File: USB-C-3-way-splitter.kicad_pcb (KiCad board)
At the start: 2 copper layers, 33 x 33 mm, 25 parts, among them J1 USB_C_Receptacle_USB2.0, J2 Conn_01x05_Socket, J3 Conn_01x05_Socket, J4 Conn_01x05_Socket, U1 LM393

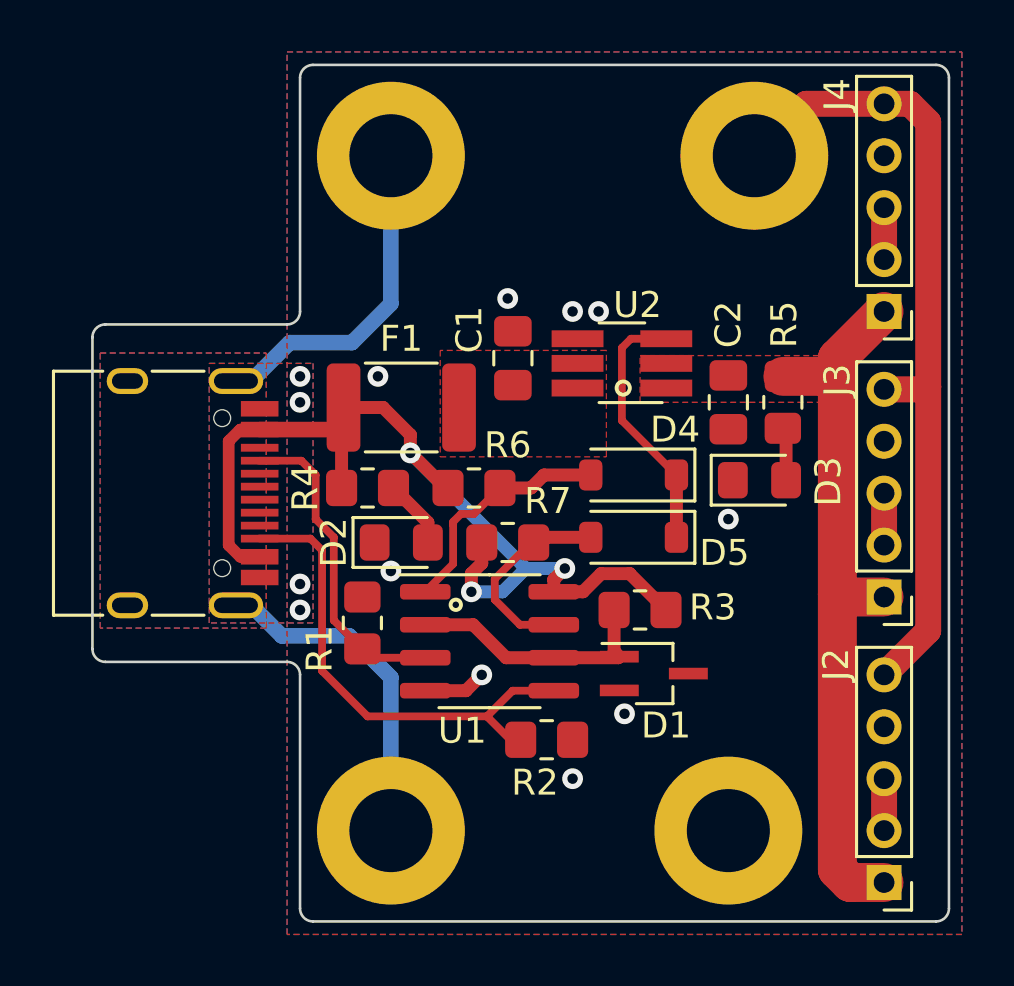
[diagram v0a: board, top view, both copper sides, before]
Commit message: Moved everything on the 5v rail to after the fuse
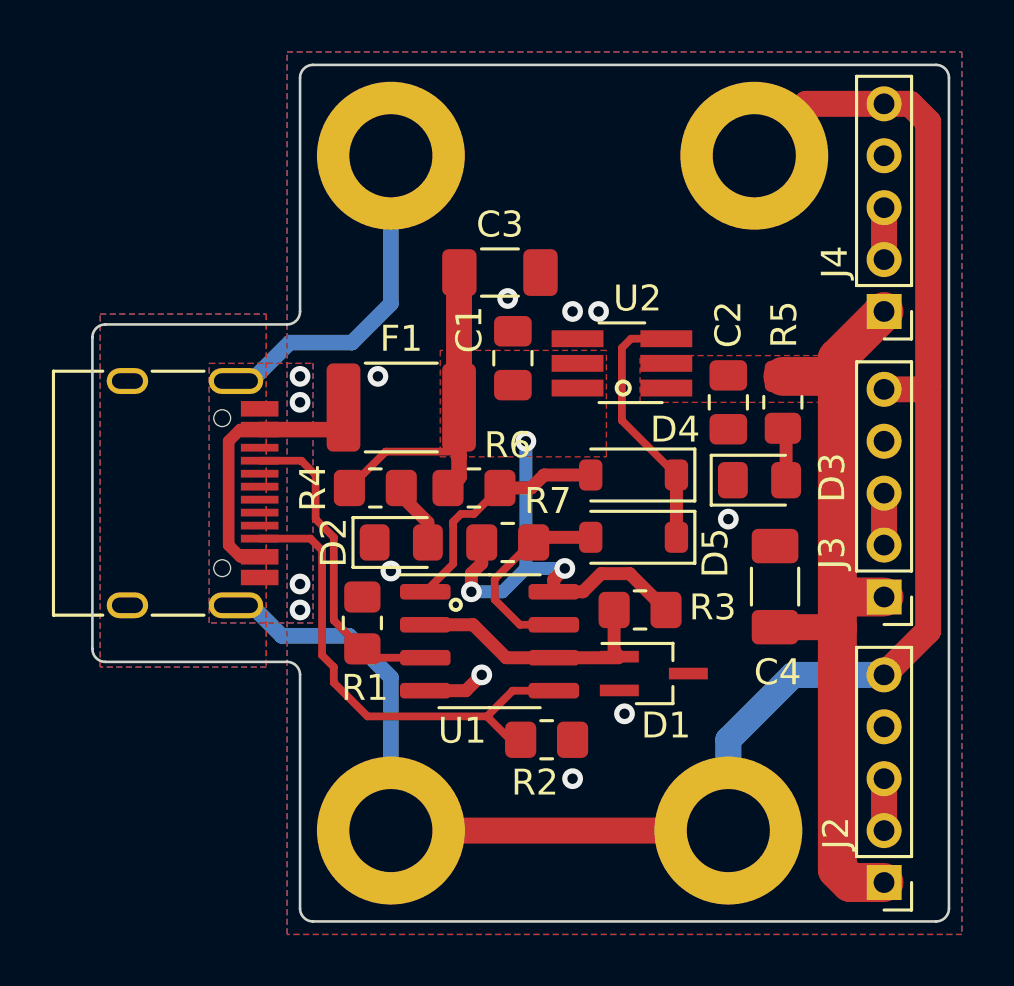
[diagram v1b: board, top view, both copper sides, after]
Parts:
- added C3: 22uF, Capacitor_SMD:C_1206_3216Metric_Pad1.33x1.80mm_HandSolder, F.Cu at (14.2, -8.50)
- added C4: 22uF, Capacitor_SMD:C_1206_3216Metric_Pad1.33x1.80mm_HandSolder, F.Cu at (24.8, 3.60)
- moved R4 0.30 mm to (9.40, -0.20)
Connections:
- C1 pad 1: Net-(C1-Pad1) -> VBUS
- F1 pad 1: VBUS -> Net-(F1-Pad1)
- F1 pad 2: Net-(C1-Pad1) -> VBUS
- J1 pad A4: VBUS -> Net-(F1-Pad1)
- J1 pad A6: D+ -> unconnected-(J1-D+-PadA6)
- J1 pad A7: D- -> unconnected-(J1-D--PadA7)
- J1 pad A9: VBUS -> Net-(F1-Pad1)
- J1 pad B4: VBUS -> Net-(F1-Pad1)
- J1 pad B6: D+ -> unconnected-(J1-D+-PadB6)
- J1 pad B7: D- -> unconnected-(J1-D--PadB7)
- J1 pad B9: VBUS -> Net-(F1-Pad1)
- U2 pad 5: Net-(C1-Pad1) -> VBUS
- U2 pad 6: Net-(C1-Pad1) -> VBUS
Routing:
- net GNDPWR: track 57.5 -> 81.0 mm
- net Net-(F1-Pad1): track 0.00 -> 11.0 mm
- net VBUS: track 38.3 -> 30.6 mm
- net +5V: track 28.3 -> 30.7 mm
- added copper zone on F.Cu, net VBUS
- removed copper zone on F.Cu, net Net-(C1-Pad1)
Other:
- board text added: "+5V"
- board text added: "D+"
- board text added: "D-"
- board text added: "GND"
- board text added: "SHIELD"

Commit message: Never mind misunderstood the LM393M's behavior
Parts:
- R6, R7: value R -> 1k
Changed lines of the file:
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@@
         (effects (font (size 1 1) (thickness 0.15)))
     )
-    (fp_text value "R" (at 0 1.65) (layer "F.Fab")
+    (fp_text value "1k" (at 0 1.65) (layer "F.Fab")
         (effects (font (size 1 1) (thickness 0.15)))
     )
@@
         (effects (font (size 1 1) (thickness 0.15)))
     )
-    (fp_text value "R" (at 0 1.65) (layer "F.Fab")
-        (effects (font (size 1 1) (thickness 0.15)))
-    )
+    (fp_text value "1k" (at 0 1.65) (layer "F.Fab")
+        (effects (font (size 1 1) (thickness 0.15)))
+    )

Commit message: Design is done maybe?
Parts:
- added C5: 100nF, Capacitor_SMD:C_0805_2012Metric_Pad1.18x1.45mm_HandSolder, F.Cu at (24.6, 7.30)
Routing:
- net +1V2: track 9.90 -> 15.3 mm
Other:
- board text added: "JLCJLCJLCJLC"
- board text added: "USB-C Splitter V1 Pylon Feb 14 24"
- board text removed: "USB-C Splitter V1 Pylon Feb 13 24"
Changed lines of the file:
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@@
     (property "ki_keywords" "cap capacitor")
     (attr smd)
-    (fp_text reference "C4" (at -3.3 0.1 180) (layer "F.SilkS")
+    (fp_text reference "C4" (at -0.7 2 270) (layer "F.SilkS")
         (effects (font (size 1 1) (thickness 0.15)))
     )
@@
       (net 1 "GND") (pintype "passive"))
     (model "${KICAD6_3DMODEL_DIR}/Resistor_SMD.3dshapes/R_0805_2012Metric.wrl"
+      (offset (xyz 0 0 0))
+      (scale (xyz 1 1 1))
+      (rotate (xyz 0 0 0))
+    )
+  )
+  (footprint "Capacitor_SMD:C_0805_2012Metric_Pad1.18x1.45mm_HandSolder" (layer "F.Cu")
+    (at 24.6 7.3)
+    (descr "Capacitor SMD 0805 (2012 Metric), square (rectangular) end terminal, IPC_7351 nominal with elongated pad for handsoldering. (Body size source: IPC-SM-782 page 76, https://www.pcb-3d.com/wordpress/wp-content/uploads/ipc-sm-782a_amendment_1_and_2.pdf, https://docs.google.com/spreadsheets/d/1BsfQQcO9C6DZCsRaXUlFlo91Tg2WpOkGARC1WS5S8t0/edit?usp=sharing), generated with kicad-footprint-generator")
+    (tags "capacitor handsolder")
+    (property "Sheetfile" "USB-C-3-way-splitter.kicad_sch")
+    (property "Sheetname" "")
+    (property "ki_description" "Unpolarized capacitor")
+    (property "ki_keywords" "cap capacitor")
+    (attr smd)
+    (fp_text reference "C5" (at 0.595 1.695) (layer "F.SilkS")
+        (effects (font (size 1 1) (thickness 0.15)))
+    )
+    (fp_text value "100nF" (at 0 1.68) (layer "F.Fab")
+        (effects (font (size 1 1) (thickness 0.15)))
+    )
+    (fp_text user "${REFERENCE}" (at 0 0) (layer "F.Fab")
+        (effects (font (size 0.5 0.5) (thickness 0.08)))
+    )
+    (fp_line (start -0.261252 -0.735) (end 0.261252 -0.735)
+      (stroke (width 0.12) (type solid)) (layer "F.SilkS"))
+    (fp_line (start -0.261252 0.735) (end 0.261252 0.735)
+      (stroke (width 0.12) (type solid)) (layer "F.SilkS"))
+    (fp_line (start -1.88 -0.98) (end 1.88 -0.98)
+      (stroke (width 0.05) (type solid)) (layer "F.CrtYd"))
+    (fp_line (start -1.88 0.98) (end -1.88 -0.98)
+      (stroke (width 0.05) (type solid)) (layer "F.CrtYd"))
+    (fp_line (start 1.88 -0.98) (end 1.88 0.98)
+      (stroke (width 0.05) (type solid)) (layer "F.CrtYd"))
+    (fp_line (start 1.88 0.98) (end -1.88 0.98)
+      (stroke (width 0.05) (type solid)) (layer "F.CrtYd"))
+    (fp_line (start -1 -0.625) (end 1 -0.625)
+      (stroke (width 0.1) (type solid)) (layer "F.Fab"))
+    (fp_line (start -1 0.625) (end -1 -0.625)
+      (stroke (width 0.1) (type solid)) (layer "F.Fab"))
+    (fp_line (start 1 -0.625) (end 1 0.625)
+      (stroke (width 0.1) (type solid)) (layer "F.Fab"))
+    (fp_line (start 1 0.625) (end -1 0.625)
+      (stroke (width 0.1) (type solid)) (layer "F.Fab"))
+    (pad "1" smd roundrect (at -1.0375 0) (size 1.175 1.45) (layers "F.Cu" "F.Paste" "F.Mask") (roundrect_rratio 0.212766)
+      (net 8 "+1V2") (pintype "passive"))
+    (pad "2" smd roundrect (at 1.0375 0) (size 1.175 1.45) (layers "F.Cu" "F.Paste" "F.Mask") (roundrect_rratio 0.212766)
+      (net 1 "GND") (pintype "passive"))
+    (model "${KICAD6_3DMODEL_DIR}/Capacitor_SMD.3dshapes/C_0805_2012Metric.wrl"
       (offset (xyz 0 0 0))
       (scale (xyz 1 1 1))
@@
   (gr_arc (start -1 6.5) (mid -1.353553 6.353553) (end -1.5 6)
     (stroke (width 0.1) (type default)) (layer "Edge.Cuts"))
+  (gr_text "JLCJLCJLCJLC" (at 21.5 -6.3 90) (layer "B.SilkS")
+    (effects (font (size 1 1) (thickness 0.2) bold) (justify left bottom mirror))
+  )
   (gr_text "+5V" (at 27.9 4.5) (layer "B.SilkS")
     (effects (font (size 1 1) (thickness 0.2) bold) (justify left bottom mirror))
@@
     (effects (font (size 1 1) (thickness 0.2) bold) (justify left bottom mirror))
   )
-  (gr_text "USB-C Splitter V1\nPylon Feb 13 24" (at 16.6 -10.5 90) (layer "B.SilkS")
+  (gr_text "USB-C Splitter V1\nPylon Feb 14 24" (at 16.6 -10.5 90) (layer "B.SilkS")
     (effects (font (size 1.5 1.5) (thickness 0.3) bold) (justify left bottom mirror))
   )
@@
   (segment (start 18.76 6.34) (end 18.8 6.3) (width 0.5) (layer "F.Cu") (net 8))
   (segment (start 16.275 6.34) (end 18.76 6.34) (width 0.5) (layer "F.Cu") (net 8))
+  (segment (start 22.2625 6) (end 23.5625 7.3) (width 0.5) (layer "F.Cu") (net 8))
+  (segment (start 18.8 6.3) (end 20 6.3) (width 0.5) (layer "F.Cu") (net 8))
   (segment (start 18.6 6.1) (end 18.8 6.3) (width 0.5) (layer "F.Cu") (net 8))
+  (segment (start 20 6.3) (end 20.3 6) (width 0.5) (layer "F.Cu") (net 8))
   (segment (start 11.325 5.07) (end 13.17 5.07) (width 0.5) (layer "F.Cu") (net 8))
   (segment (start 14.44 6.34) (end 16.275 6.34) (width 0.5) (layer "F.Cu") (net 8))
+  (segment (start 20.3 6) (end 22.2625 6) (width 0.5) (layer "F.Cu") (net 8))
   (segment (start 13.17 5.07) (end 14.44 6.34) (width 0.5) (layer "F.Cu") (net 8))
   (segment (start 11.425 1.125) (end 11.425 1.9) (width 0.5) (layer "F.Cu") (net 9))

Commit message: Added JLCPCB tooling holes
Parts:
- added H5: MountingHole, USB-C-3-way-splitter-footprints:JLCPCB-tooling-hole, F.Cu at (14.5, -15.0)
- added H6: MountingHole, USB-C-3-way-splitter-footprints:JLCPCB-tooling-hole, F.Cu at (14.0, 15.0)
- added H7: MountingHole, USB-C-3-way-splitter-footprints:JLCPCB-tooling-hole, F.Cu at (26.0, -8.00)
- U2: value ~ -> SiP32509
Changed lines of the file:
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@@
     )
+  )
+  (footprint "USB-C-3-way-splitter-footprints:JLCPCB-tooling-hole" (layer "F.Cu")
+    (at 26 -8)
+    (property "Sheetfile" "USB-C-3-way-splitter.kicad_sch")
+    (property "Sheetname" "")
+    (property "ki_description" "Mounting Hole without connection")
+    (property "ki_keywords" "mounting hole")
+    (attr smd)
+    (fp_text reference "H7" (at 0 -2 unlocked) (layer "User.1")
+        (effects (font (size 1 1) (thickness 0.1)))
+    )
+    (fp_text value "MountingHole" (at 0 1 unlocked) (layer "F.Fab")
+        (effects (font (size 1 1) (thickness 0.15)))
+    )
+    (fp_text user "${REFERENCE}" (at 0 2.5 unlocked) (layer "F.Fab")
+        (effects (font (size 1 1) (thickness 0.15)))
+    )
+    (pad "" np_thru_hole circle (at 0 0) (size 2.286 2.286) (drill 1.152) (layers "F&B.Cu" "*.Mask")
+      (solder_mask_margin 0.148) (clearance 0.148))
   )
   (footprint "Diode_SMD:D_SOD-123" (layer "F.Cu")
@@
     (pad "1" thru_hole circle (at 0 0) (size 5.7 5.7) (drill 3.2) (layers "*.Cu" "*.Mask")
       (net 16 "GNDPWR") (pinfunction "1") (pintype "input"))
+  )
+  (footprint "USB-C-3-way-splitter-footprints:JLCPCB-tooling-hole" (layer "F.Cu")
+    (at 14 15)
+    (property "Sheetfile" "USB-C-3-way-splitter.kicad_sch")
+    (property "Sheetname" "")
+    (property "ki_description" "Mounting Hole without connection")
+    (property "ki_keywords" "mounting hole")
+    (attr smd)
+    (fp_text reference "H6" (at 0 -2 unlocked) (layer "User.1")
+        (effects (font (size 1 1) (thickness 0.1)))
+    )
+    (fp_text value "MountingHole" (at 0 1 unlocked) (layer "F.Fab")
+        (effects (font (size 1 1) (thickness 0.15)))
+    )
+    (fp_text user "${REFERENCE}" (at 0 2.5 unlocked) (layer "F.Fab")
+        (effects (font (size 1 1) (thickness 0.15)))
+    )
+    (pad "" np_thru_hole circle (at 0 0) (size 2.286 2.286) (drill 1.152) (layers "F&B.Cu" "*.Mask")
+      (solder_mask_margin 0.148) (clearance 0.148))
   )
   (footprint "Package_SO:SOIC-8_3.9x4.9mm_P1.27mm" (layer "F.Cu")
@@
         (effects (font (size 1 1) (thickness 0.15)))
     )
-    (fp_text value "~" (at 0 2.5) (layer "F.Fab")
+    (fp_text value "SiP32509" (at 0 2.5) (layer "F.Fab")
         (effects (font (size 1 1) (thickness 0.15)))
     )
@@
     (fp_line (start 1 0.625) (end -1 0.625)
       (stroke (width 0.1) (type solid)) (layer "F.Fab"))
-    (pad "1" smd roundrect (at -1.0375 0) (size 1.175 1.45) (layers "F.Cu" "F.Paste" "F.Mask") (roundrect_rratio 0.212766)
+    (pad "1" smd roundrect (at -1.0375 0) (size 1.175 1.45) (layers "F.Cu" "F.Paste" "F.Mask") (roundrect_rratio 0.2127659574)
       (net 8 "+1V2") (pintype "passive"))
-    (pad "2" smd roundrect (at 1.0375 0) (size 1.175 1.45) (layers "F.Cu" "F.Paste" "F.Mask") (roundrect_rratio 0.212766)
+    (pad "2" smd roundrect (at 1.0375 0) (size 1.175 1.45) (layers "F.Cu" "F.Paste" "F.Mask") (roundrect_rratio 0.2127659574)
       (net 1 "GND") (pintype "passive"))
     (model "${KICAD6_3DMODEL_DIR}/Capacitor_SMD.3dshapes/C_0805_2012Metric.wrl"
@@
     )
   )
+  (footprint "USB-C-3-way-splitter-footprints:JLCPCB-tooling-hole" (layer "F.Cu")
+    (at 14.5 -15)
+    (property "Sheetfile" "USB-C-3-way-splitter.kicad_sch")
+    (property "Sheetname" "")
+    (property "ki_description" "Mounting Hole without connection")
+    (property "ki_keywords" "mounting hole")
+    (attr smd)
+    (fp_text reference "H5" (at 0 -2 unlocked) (layer "User.1")
+        (effects (font (size 1 1) (thickness 0.1)))
+    )
+    (fp_text value "MountingHole" (at 0 1 unlocked) (layer "F.Fab")
+        (effects (font (size 1 1) (thickness 0.15)))
+    )
+    (fp_text user "${REFERENCE}" (at 0 2.5 unlocked) (layer "F.Fab")
+        (effects (font (size 1 1) (thickness 0.15)))
+    )
+    (pad "" np_thru_hole circle (at 0 0) (size 2.286 2.286) (drill 1.152) (layers "F&B.Cu" "*.Mask")
+      (solder_mask_margin 0.148) (clearance 0.148))
+  )
   (footprint "Fuse:Fuse_1812_4532Metric_Pad1.30x3.40mm_HandSolder" (layer "F.Cu")

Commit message: Added pulldown to EN, added test points
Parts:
- added R8: 100k, Resistor_SMD:R_0805_2012Metric_Pad1.20x1.40mm_HandSolder, F.Cu at (19.0, -10.0)
- added TP1: TestPoint, TestPoint:TestPoint_Pad_D2.5mm, B.Cu at (9.00, -1.70)
- added TP2: TestPoint, TestPoint:TestPoint_Pad_D2.5mm, B.Cu at (8.10, 1.90)
- added TP3: TestPoint, TestPoint:TestPoint_Pad_D2.5mm, B.Cu at (22.6, -8.00)
- added TP4: TestPoint, TestPoint:TestPoint_Pad_D2.5mm, B.Cu at (22.6, 5.20)
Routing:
- net EN: track 10.0 -> 16.0 mm, vias 0 -> 1
- net CC1: track 12.4 -> 14.7 mm, vias 0 -> 1
- net CC2: track 19.0 -> 20.8 mm, vias 0 -> 1
- net +1V2: vias 0 -> 1
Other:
- board text added: "1.25V"
- board text added: "CC1"
- board text added: "CC2"
- board text added: "EN"

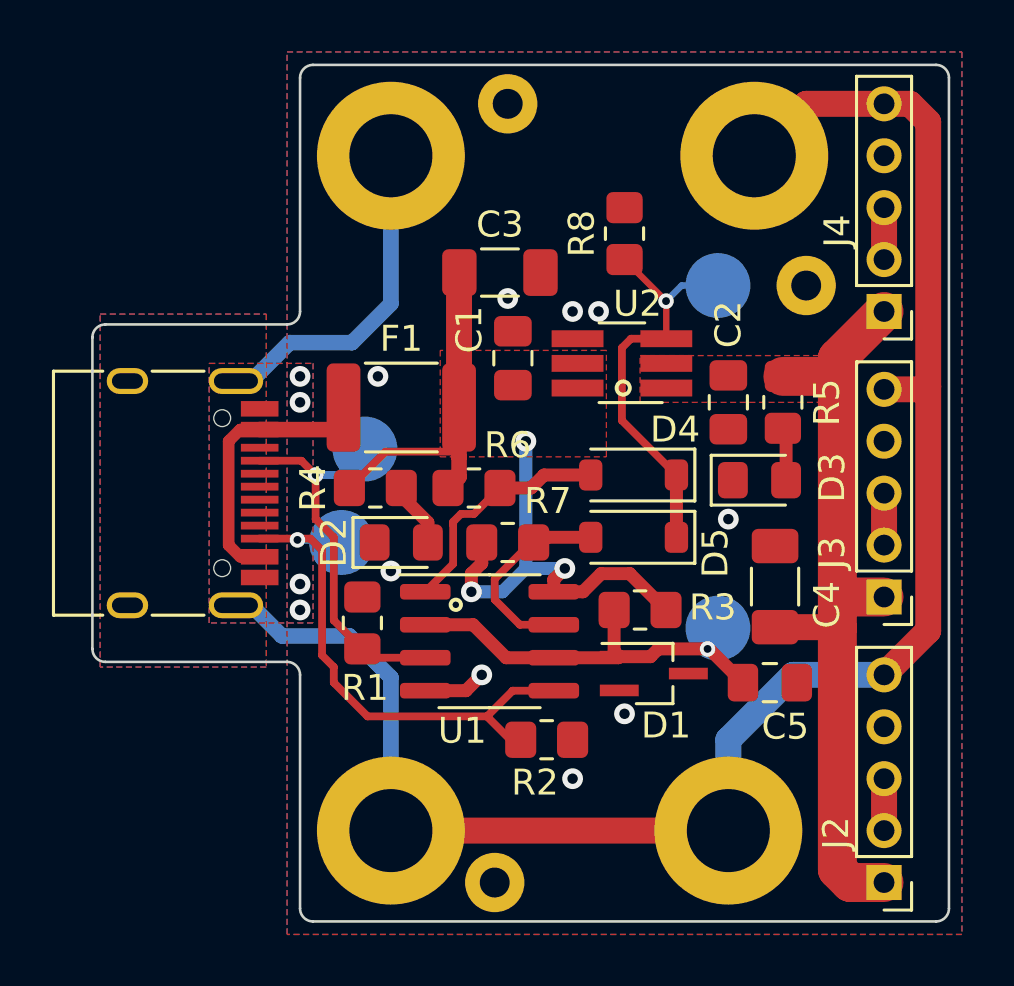
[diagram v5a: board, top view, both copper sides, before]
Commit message: Removed unnecessary diodes and resistor
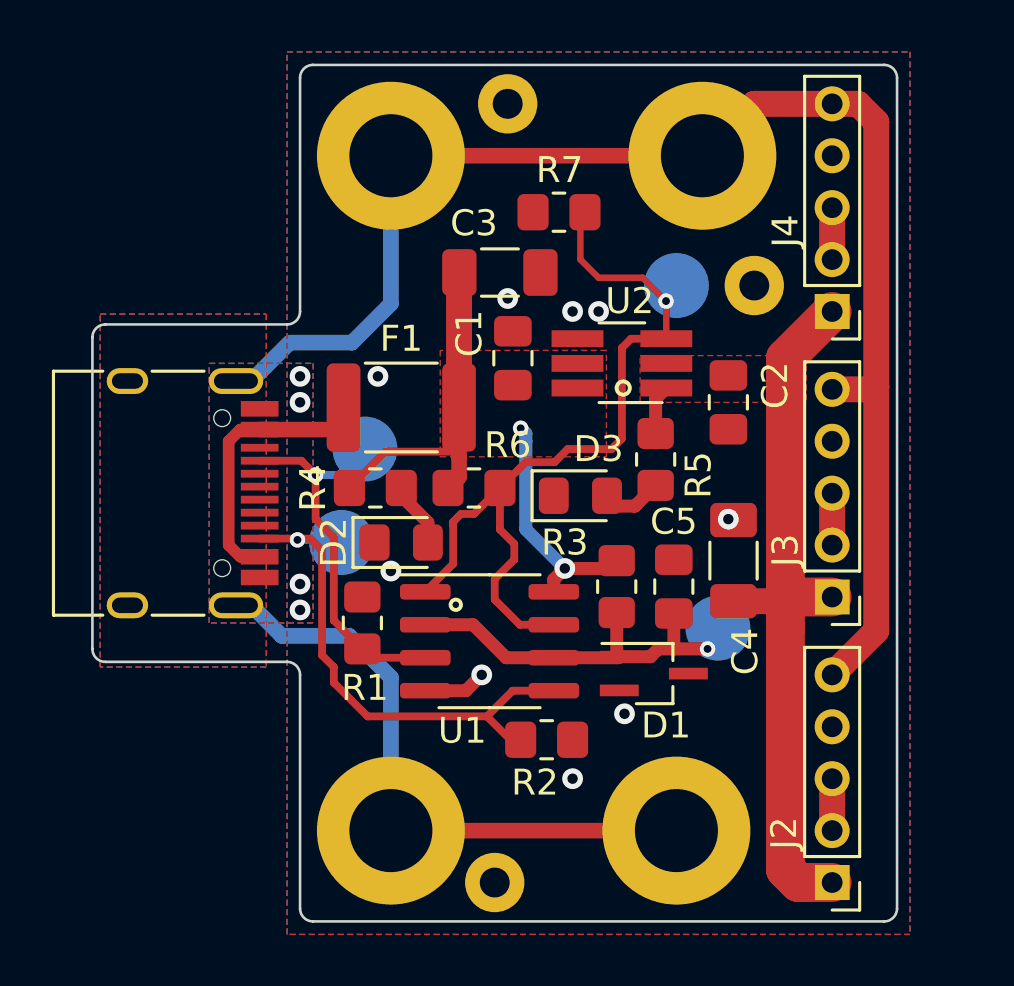
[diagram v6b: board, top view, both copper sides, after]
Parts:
- removed D4, D5: 1N4148W, Diode_SMD:D_SOD-123
- removed R8: 100k, Resistor_SMD:R_0805_2012Metric_Pad1.20x1.40mm_HandSolder
- R7: value 1k -> 100k
- moved R7 12.9 mm to (16.5, -10.8), turned to 180 degrees
- moved D3 6.93 mm to (17.3, 0.10)
- moved R5 5.37 mm to (20.2, -1.30)
- moved C5 5.23 mm to (20.9, 3.60), turned to 90 degrees
- moved H2 2.00 mm to (22.0, -13.0)
- moved H4 2.00 mm to (21.0, 13.0)
- moved H7 2.00 mm to (24.0, -8.00)
- moved J2 2.00 mm to (27.0, 15.0)
- moved J3 2.00 mm to (27.0, 4.00)
- moved J4 2.00 mm to (27.0, -7.00)
- moved C4 1.89 mm to (23.2, 2.60)
- moved TP3 1.60 mm to (21.0, -8.00)
- moved R3 1.27 mm to (18.7, 3.60), turned to -90 degrees
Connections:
- R6 pad 2: Net-(D4-A) -> EN
- R7 pad 1: VBUS -> EN
- R7 pad 2: Net-(D5-A) -> GND
- U1 pad 1: Net-(D4-A) -> EN
- U1 pad 7: Net-(D5-A) -> EN
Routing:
- net EN: track 16.0 -> 31.1 mm
- net Net-(D4-A): track 9.19 -> 0.00 mm
- net VBUS: track 30.6 -> 22.7 mm, vias 3 -> 2
- net Net-(D5-A): track 7.39 -> 0.00 mm
- net +1V2: track 15.3 -> 14.6 mm
- net +5V: track 30.7 -> 30.2 mm
- net GNDPWR: track 81.0 -> 80.5 mm
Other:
- board size 33 x 33 mm -> 31 x 33 mm
- board text added: "5V"
- board text added: "USB-C Splitter V1 Pylon Feb 15 24"
- board text removed: "+5V"
- board text removed: "USB-C Splitter V1 Pylon Feb 14 24"
